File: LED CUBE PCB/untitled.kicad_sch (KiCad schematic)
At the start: 46 parts, among them J1 Conn_01x06, J3 Conn_01x09, SW1 BZCN_TSA007A1518B03, U1 TPS7A2633DRVR, U2 CH340C, Y3 8MHz

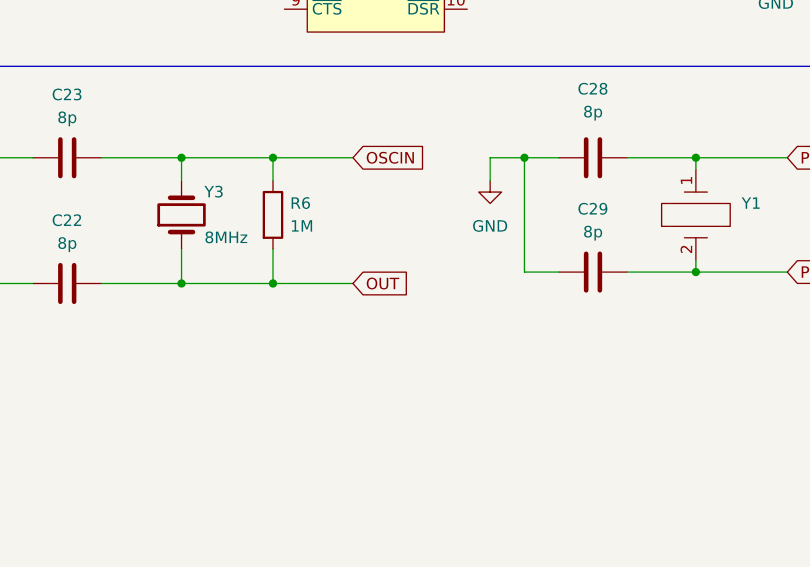
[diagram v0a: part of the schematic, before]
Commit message: Added ground filled zone on PCB
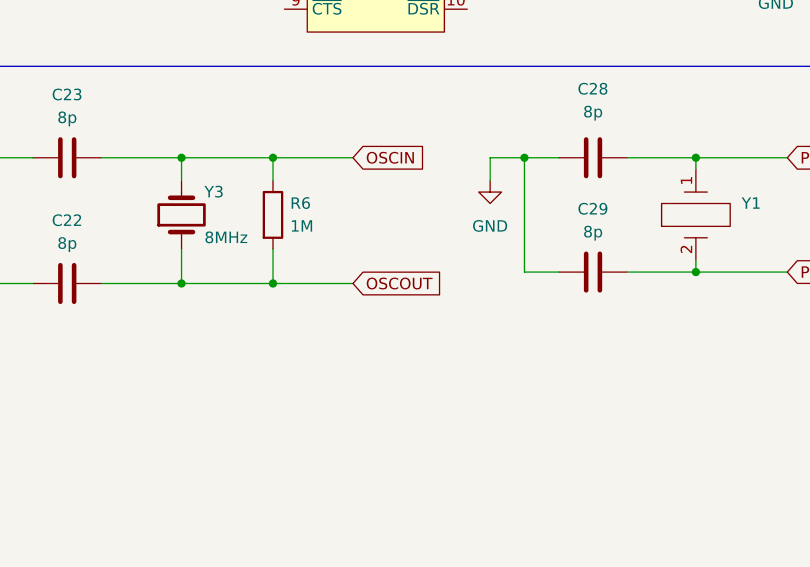
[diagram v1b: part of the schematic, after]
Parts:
- Y3: footprint Crystal:Crystal_Round_D3.0mm_Vertical -> Marina_Library:ECS-080-18-23G-JGN-TR
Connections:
- net OUT is gone; now on net OSCOUT: C22.1, R6.2, Y3.1
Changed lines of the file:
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@@
 		)
 	)
-	(global_label "OUT"
+	(global_label "OSCOUT"
 		(shape input)
 		(at 220.98 162.56 0)
@@
 		)
 		(property "Intersheetrefs" "${INTERSHEET_REFS}"
-			(at 227.5938 162.56 0)
+			(at 231.4038 162.56 0)
 			(effects
 				(font
@@
 			)
 		)
-		(property "Footprint" "Crystal:Crystal_Round_D3.0mm_Vertical"
+		(property "Footprint" "Marina_Library:ECS-080-18-23G-JGN-TR"
 			(at 201.93 154.94 0)
 			(effects

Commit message: Updated PCB - Marina
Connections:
- net +3V3 is gone; now on net 3V3: R10.1
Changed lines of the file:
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@@
 	(wire
 		(pts
+			(xy 152.4 20.32) (xy 154.94 20.32)
+		)
+		(stroke
+			(width 0)
+			(type default)
+		)
+	)
+	(wire
+		(pts
 			(xy 152.4 101.6) (xy 144.78 101.6)
 		)
@@
 	(wire
 		(pts
-			(xy 152.4 27.94) (xy 152.4 24.13)
+			(xy 152.4 20.32) (xy 152.4 27.94)
 		)
 		(stroke
@@
 	(wire
 		(pts
-			(xy 25.4 38.1) (xy 25.4 40.64)
-		)
-		(stroke
-			(width 0)
-			(type default)
-		)
-	)
-	(wire
-		(pts
 			(xy 142.24 107.95) (xy 138.43 107.95)
 		)
@@
 		)
 	)
+	(global_label "GND"
+		(shape input)
+		(at 25.4 38.1 180)
+		(fields_autoplaced yes)
+		(effects
+			(font
+				(size 1.27 1.27)
+			)
+			(justify right)
+		)
+		(property "Intersheetrefs" "${INTERSHEET_REFS}"
+			(at 18.5443 38.1 0)
+			(effects
+				(font
+					(size 1.27 1.27)
+				)
+				(justify right)
+				(hide yes)
+			)
+		)
+	)
 	(global_label "5V"
 		(shape input)
@@
 		)
 	)
+	(global_label "3V3"
+		(shape input)
+		(at 154.94 20.32 0)
+		(fields_autoplaced yes)
+		(effects
+			(font
+				(size 1.27 1.27)
+			)
+			(justify left)
+		)
+		(property "Intersheetrefs" "${INTERSHEET_REFS}"
+			(at 161.4328 20.32 0)
+			(effects
+				(font
+					(size 1.27 1.27)
+				)
+				(justify left)
+				(hide yes)
+			)
+		)
+	)
 	(global_label "PB3"
 		(shape input)
@@
 	)
 	(symbol
-		(lib_id "power:+3V3")
-		(at 152.4 24.13 0)
-		(unit 1)
-		(exclude_from_sim no)
-		(in_bom yes)
-		(on_board yes)
-		(dnp no)
-		(fields_autoplaced yes)
-		(property "Reference" "#PWR036"
-			(at 152.4 27.94 0)
-			(effects
-				(font
-					(size 1.27 1.27)
-				)
-				(hide yes)
-			)
-		)
-		(property "Value" "+3V3"
-			(at 152.4 19.685 0)
-			(effects
-				(font
-					(size 1.27 1.27)
-				)
-			)
-		)
-		(property "Footprint" ""
-			(at 152.4 24.13 0)
-			(effects
-				(font
-					(size 1.27 1.27)
-				)
-				(hide yes)
-			)
-		)
-		(property "Datasheet" ""
-			(at 152.4 24.13 0)
-			(effects
-				(font
-					(size 1.27 1.27)
-				)
-				(hide yes)
-			)
-		)
-		(property "Description" ""
-			(at 152.4 24.13 0)
-			(effects
-				(font
-					(size 1.27 1.27)
-				)
-			)
-		)
-		(pin "1"
-		)
-		(instances
-			(project "LED CUBE PCB"
-				(path "/64eb2d32-222b-4351-90b6-2cc90b760e62/ccca4637-6427-4f45-abce-b48cba1912e2"
-					(reference "#PWR036")
-					(unit 1)
-				)
-			)
-		)
-	)
-	(symbol
 		(lib_name "GND_2")
 		(lib_id "power:GND")
@@
 					(unit 1)
 				)
-			)
-		)
-	)
-	(symbol
-		(lib_name "GND_1")
-		(lib_id "power:GND")
-		(at 25.4 40.64 0)
-		(unit 1)
-		(exclude_from_sim no)
-		(in_bom yes)
-		(on_board yes)
-		(dnp no)
-		(fields_autoplaced yes)
-		(property "Reference" "#PWR01"
-			(at 25.4 46.99 0)
-			(effects
-				(font
-					(size 1.27 1.27)
-				)
-				(hide yes)
-			)
-		)
-		(property "Value" "GND"
-			(at 25.4 45.72 0)
-			(effects
-				(font
-					(size 1.27 1.27)
-				)
-			)
-		)
-		(property "Footprint" ""
-			(at 25.4 40.64 0)
-			(effects
-				(font
-					(size 1.27 1.27)
-				)
-				(hide yes)
-			)
-		)
-		(property "Datasheet" ""
-			(at 25.4 40.64 0)
-			(effects
-				(font
-					(size 1.27 1.27)
-				)
-				(hide yes)
-			)
-		)
-		(property "Description" "Power symbol creates a global label with name \"GND\" , ground"
-			(at 25.4 40.64 0)
-			(effects
-				(font
-					(size 1.27 1.27)
-				)
-				(hide yes)
-			)
-		)
-		(pin "1"
-		)
-		(instances
-			(project ""
-				(path "/64eb2d32-222b-4351-90b6-2cc90b760e62/ccca4637-6427-4f45-abce-b48cba1912e2"
-					(reference "#PWR01")
-					(unit 1)
-				)

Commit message: PCB is finish
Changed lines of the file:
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@@
 	(wire
 		(pts
+			(xy 22.86 38.1) (xy 22.86 39.37)
+		)
+		(stroke
+			(width 0)
+			(type default)
+		)
+	)
+	(wire
+		(pts
 			(xy 96.52 33.02) (xy 114.3 33.02)
 		)
@@
 	(wire
 		(pts
-			(xy 152.4 35.56) (xy 152.4 38.1)
+			(xy 30.48 38.1) (xy 22.86 38.1)
 		)
 		(stroke
@@
 	(wire
 		(pts
-			(xy 124.46 88.9) (xy 130.81 88.9)
+			(xy 152.4 35.56) (xy 152.4 38.1)
 		)
 		(stroke
@@
 	(wire
 		(pts
-			(xy 201.93 148.59) (xy 212.09 148.59)
+			(xy 124.46 88.9) (xy 130.81 88.9)
 		)
 		(stroke
@@
 	(wire
 		(pts
-			(xy 193.04 148.59) (xy 201.93 148.59)
+			(xy 201.93 148.59) (xy 212.09 148.59)
 		)
 		(stroke
@@
 	(wire
 		(pts
-			(xy 149.86 85.09) (xy 149.86 91.44)
+			(xy 193.04 148.59) (xy 201.93 148.59)
 		)
 		(stroke
@@
 	(wire
 		(pts
-			(xy 194.31 127) (xy 213.36 127)
+			(xy 149.86 85.09) (xy 149.86 91.44)
 		)
 		(stroke
@@
 	(wire
 		(pts
-			(xy 44.45 168.91) (xy 41.91 168.91)
+			(xy 194.31 127) (xy 213.36 127)
 		)
 		(stroke
@@
 	(wire
 		(pts
-			(xy 30.48 38.1) (xy 25.4 38.1)
+			(xy 44.45 168.91) (xy 41.91 168.91)
 		)
 		(stroke
@@
 		)
 	)
-	(global_label "GND"
-		(shape input)
-		(at 25.4 38.1 180)
-		(fields_autoplaced yes)
-		(effects
-			(font
-				(size 1.27 1.27)
-			)
-			(justify right)
-		)
-		(property "Intersheetrefs" "${INTERSHEET_REFS}"
-			(at 18.5443 38.1 0)
-			(effects
-				(font
-					(size 1.27 1.27)
-				)
-				(justify right)
-				(hide yes)
-			)
-		)
-	)
 	(global_label "5V"
 		(shape input)
@@
 					(unit 1)
 				)
+			)
+		)
+	)
+	(symbol
+		(lib_name "GND_2")
+		(lib_id "power:GND")
+		(at 22.86 39.37 0)
+		(unit 1)
+		(exclude_from_sim no)
+		(in_bom yes)
+		(on_board yes)
+		(dnp no)
+		(fields_autoplaced yes)
+		(property "Reference" "#PWR01"
+			(at 22.86 45.72 0)
+			(effects
+				(font
+					(size 1.27 1.27)
+				)
+				(hide yes)
+			)
+		)
+		(property "Value" "GND"
+			(at 22.86 44.45 0)
+			(effects
+				(font
+					(size 1.27 1.27)
+				)
+			)
+		)
+		(property "Footprint" ""
+			(at 22.86 39.37 0)
+			(effects
+				(font
+					(size 1.27 1.27)
+				)
+				(hide yes)
+			)
+		)
+		(property "Datasheet" ""
+			(at 22.86 39.37 0)
+			(effects
+				(font
+					(size 1.27 1.27)
+				)
+				(hide yes)
+			)
+		)
+		(property "Description" "Power symbol creates a global label with name \"GND\" , ground"
+			(at 22.86 39.37 0)
+			(effects
+				(font
+					(size 1.27 1.27)
+				)
+				(hide yes)
+			)
+		)
+		(pin "1"
+		)
+		(instances
+			(project "LED CUBE PCB"
+				(path "/64eb2d32-222b-4351-90b6-2cc90b760e62/ccca4637-6427-4f45-abce-b48cba1912e2"
+					(reference "#PWR01")
+					(unit 1)
+				)

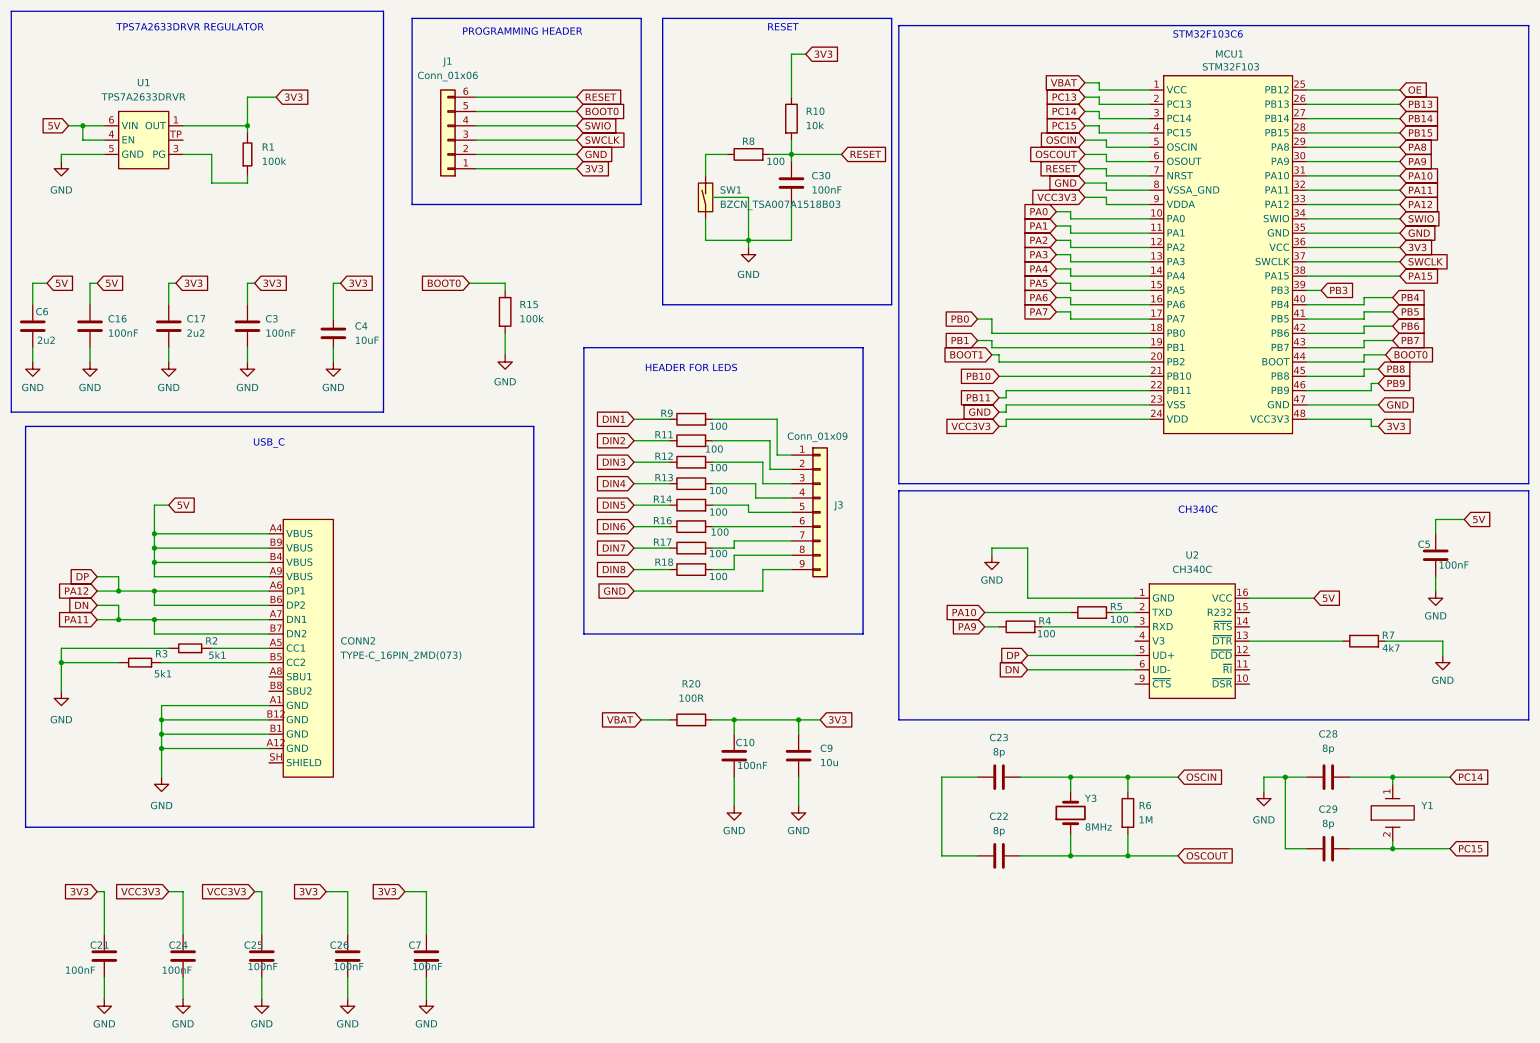
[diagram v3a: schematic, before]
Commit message: Solved problem with VCC3V3 and 3V3 on schematic
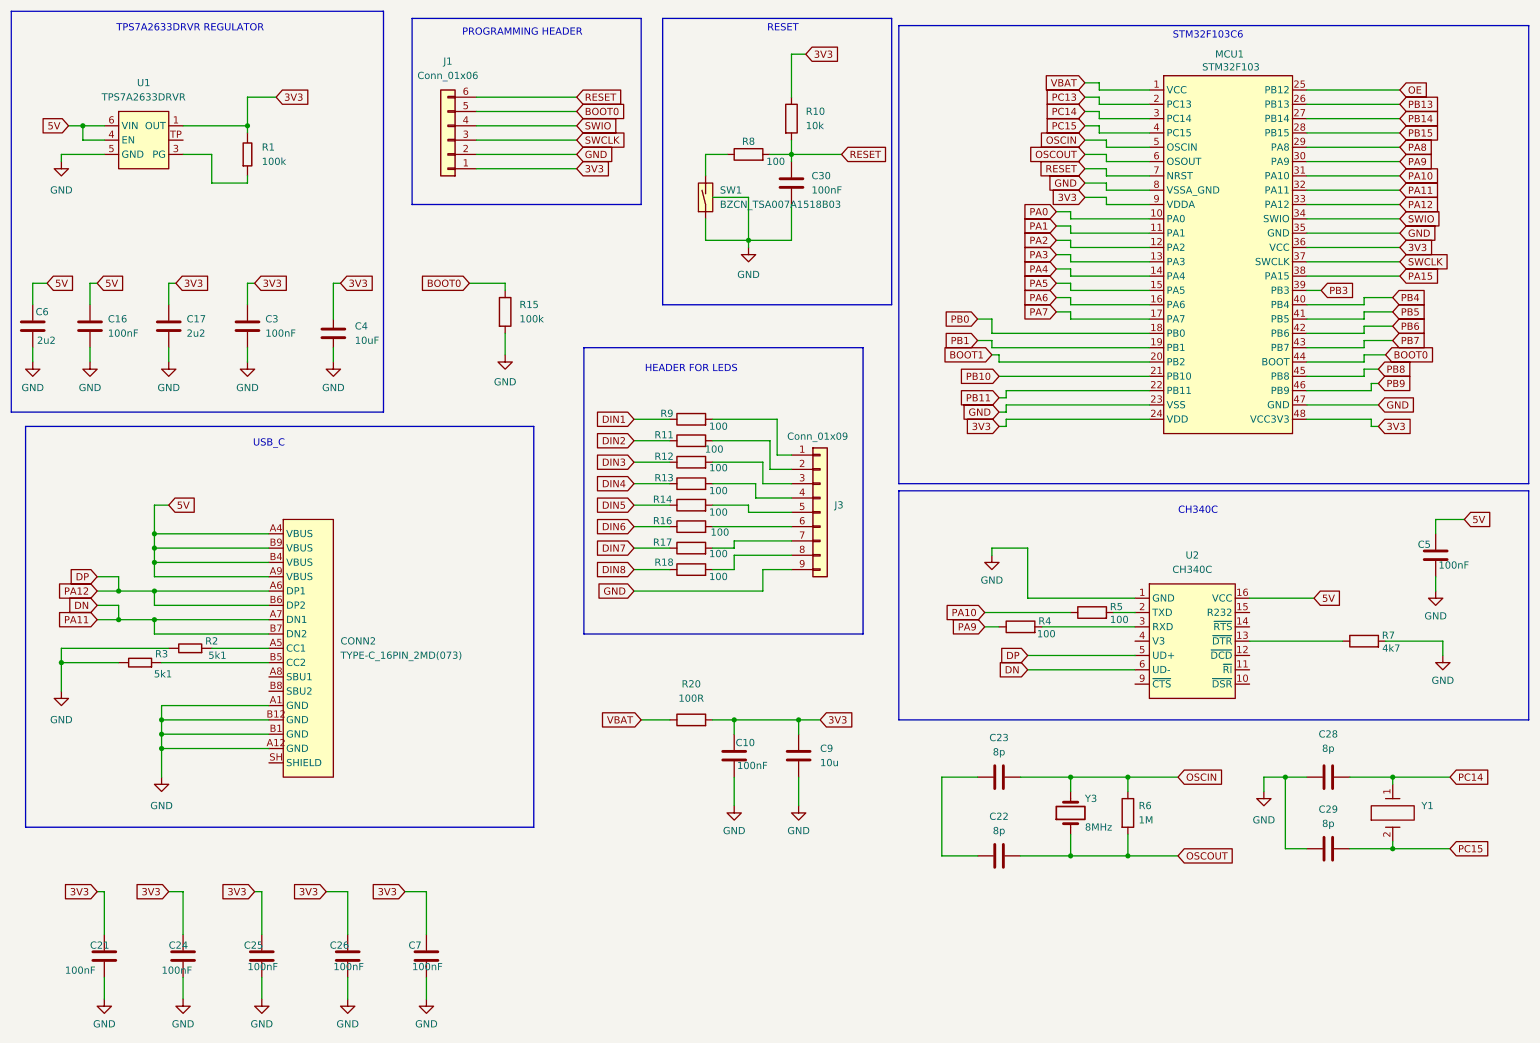
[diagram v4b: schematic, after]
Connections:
- net VCC3V3 is gone; now on net 3V3: C24.1, C25.1, MCU1.24 (VDD), MCU1.9 (VDDA)
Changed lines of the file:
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@@
 		)
 	)
-	(global_label "VCC3V3"
+	(global_label "3V3"
 		(shape input)
 		(at 189.23 86.36 180)
@@
 		)
 		(property "Intersheetrefs" "${INTERSHEET_REFS}"
-			(at 179.1086 86.36 0)
+			(at 182.7372 86.36 0)
 			(effects
 				(font
@@
 		)
 	)
-	(global_label "VCC3V3"
+	(global_label "3V3"
 		(shape input)
 		(at 41.91 168.91 180)
@@
 		)
 		(property "Intersheetrefs" "${INTERSHEET_REFS}"
-			(at 31.7886 168.91 0)
+			(at 35.4172 168.91 0)
 			(effects
 				(font
@@
 		)
 	)
-	(global_label "VCC3V3"
+	(global_label "3V3"
 		(shape input)
 		(at 204.47 45.72 180)
@@
 		)
 		(property "Intersheetrefs" "${INTERSHEET_REFS}"
-			(at 194.3486 45.72 0)
+			(at 197.9772 45.72 0)
 			(effects
 				(font
@@
 		)
 	)
-	(global_label "VCC3V3"
+	(global_label "3V3"
 		(shape input)
 		(at 57.15 168.91 180)
@@
 		)
 		(property "Intersheetrefs" "${INTERSHEET_REFS}"
-			(at 47.0286 168.91 0)
-			(effects
-				(font
+			(at 50.6572 168.91 0)
+			(effects
+				(font
